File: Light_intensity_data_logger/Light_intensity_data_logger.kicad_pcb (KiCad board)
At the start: 2 copper layers, 23 parts, among them J1 Wire_to_Vbat, Q1 NTJD4001NT1G, Q2 NTJD4001NT1G, U1 BME280, U2 TSL25911FN, U3 TCS34725FN, U4 Teensy3.6

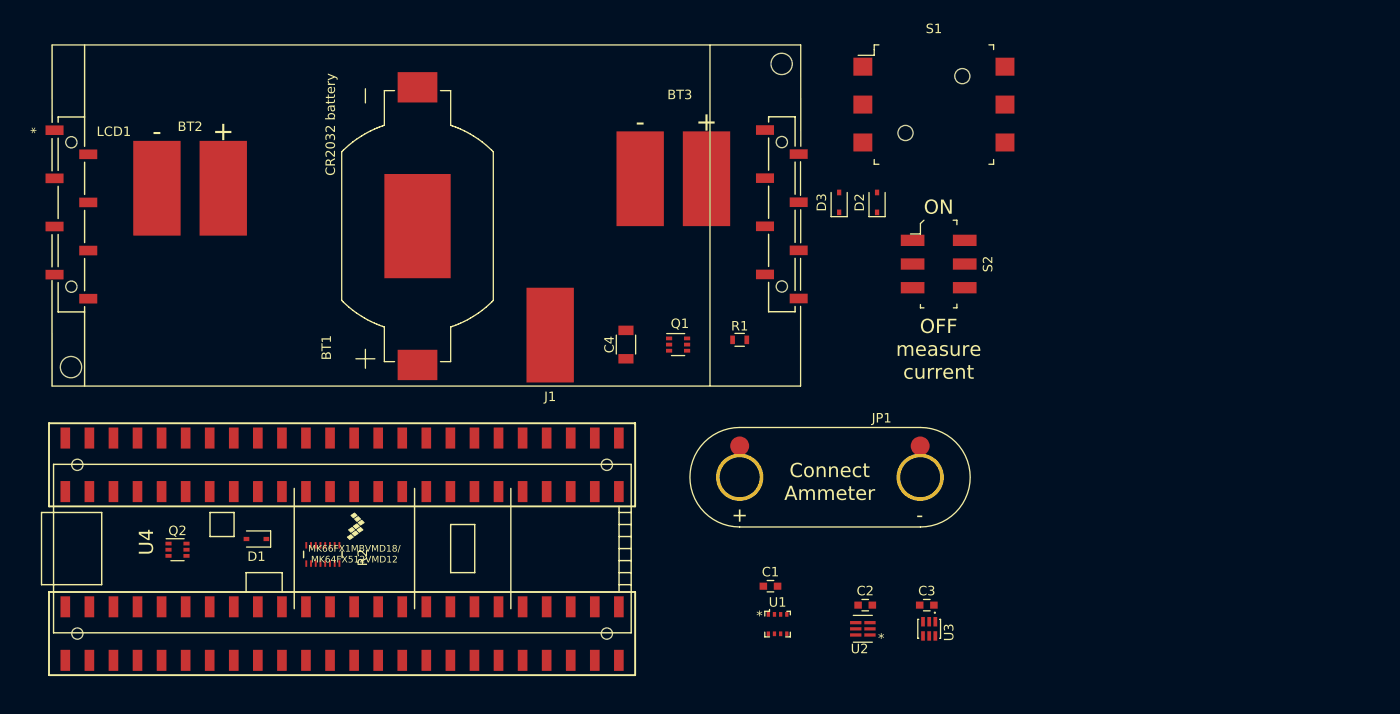
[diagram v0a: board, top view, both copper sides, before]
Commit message: Sensors connected in PCB layout
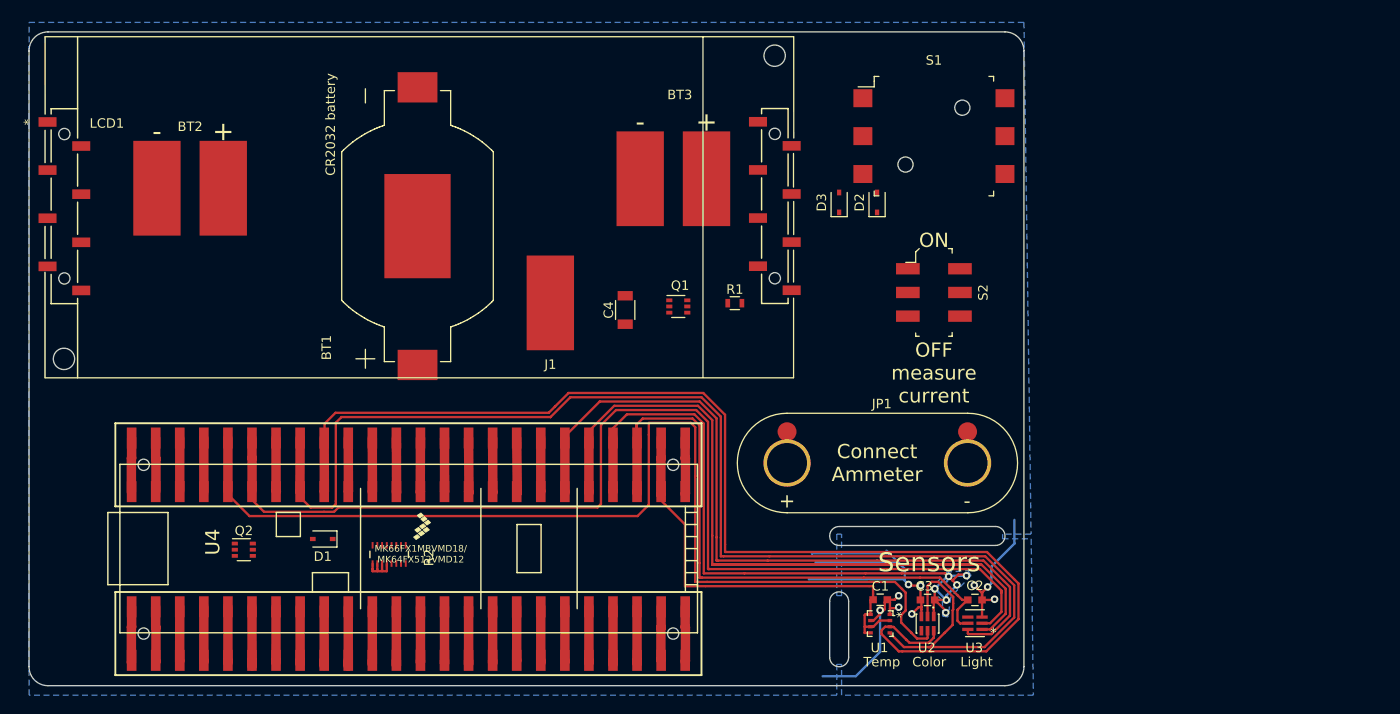
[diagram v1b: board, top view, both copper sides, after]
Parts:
- R2: value EXB-2HV103JV_-_8x10k_resistor_array -> EXB-2HV472JV_-_8x4.7k_resistor_array
- moved U3 11.8 mm to (172.8, 94.4)
- moved C1 11.7 mm to (162.8, 91.9), turned to 180 degrees
- moved C2 11.6 mm to (172.8, 92.0)
- moved U1 10.8 mm to (162.8, 94.5), turned to 270 degrees
- moved D1 7.00 mm to (104.0, 85.5)
- moved Q2 7.00 mm to (95.7, 86.7)
- moved R2 7.00 mm to (111.0, 87.2)
- moved U4 7.00 mm to (82.0, 100.0)
- moved JP1 5.22 mm to (153.0, 77.5)
- moved Q1 4.02 mm to (141.5, 61.0)
- moved R1 3.90 mm to (147.5, 60.6)
- moved C4 3.65 mm to (135.9, 61.4)
- moved J1 3.40 mm to (128.0, 60.6)
- moved S1 3.33 mm to (168.5, 43.0)
- moved S2 3.04 mm to (168.5, 59.5)
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- renumbered U3 to U2, U2 to U3
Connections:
- R2 pad 5: /SDA2 -> /SDA0
- R2 pad 6: /SCL2 -> /SCL0
- U2 pad 2: /SCL2 -> /SCL0
- U2 pad 6: /SDA2 -> /SDA0
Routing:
- net /SCL0: track 0.00 -> 140.5 mm
- net /SCL1: track 0.00 -> 130.9 mm
- net /SDA0: track 0.00 -> 127.1 mm
- net /21*: track 0.00 -> 117.3 mm
- net /22*: track 0.00 -> 112.0 mm
- net GND: track 0.00 -> 89.3 mm, vias 0 -> 9
- net /SDA1: track 0.00 -> 80.0 mm
- net /36: track 0.00 -> 76.5 mm, vias 0 -> 6
- net /35: track 0.00 -> 65.4 mm
- net /34: track 0.00 -> 45.0 mm
- net /3v3: track 0.00 -> 12.1 mm
- net /I2C_Pullup: track 0.00 -> 11.1 mm
- net Net-(U4-Pad10): track 0.00 -> 6.88 mm
- net /SDA2: track 0.00 -> 6.82 mm
- net /7*: track 0.00 -> 6.76 mm
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- added copper zone on B.Cu, net /36
- added copper zone on B.Cu, net GND
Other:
- board outline added: 105 x 69 mm
- board text added: "CUTOUT"
- board text added: "Color"
- board text added: "Light"
- board text added: "Sensors"
- board text added: "Temp"

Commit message: Teensy flipped sensors rewired
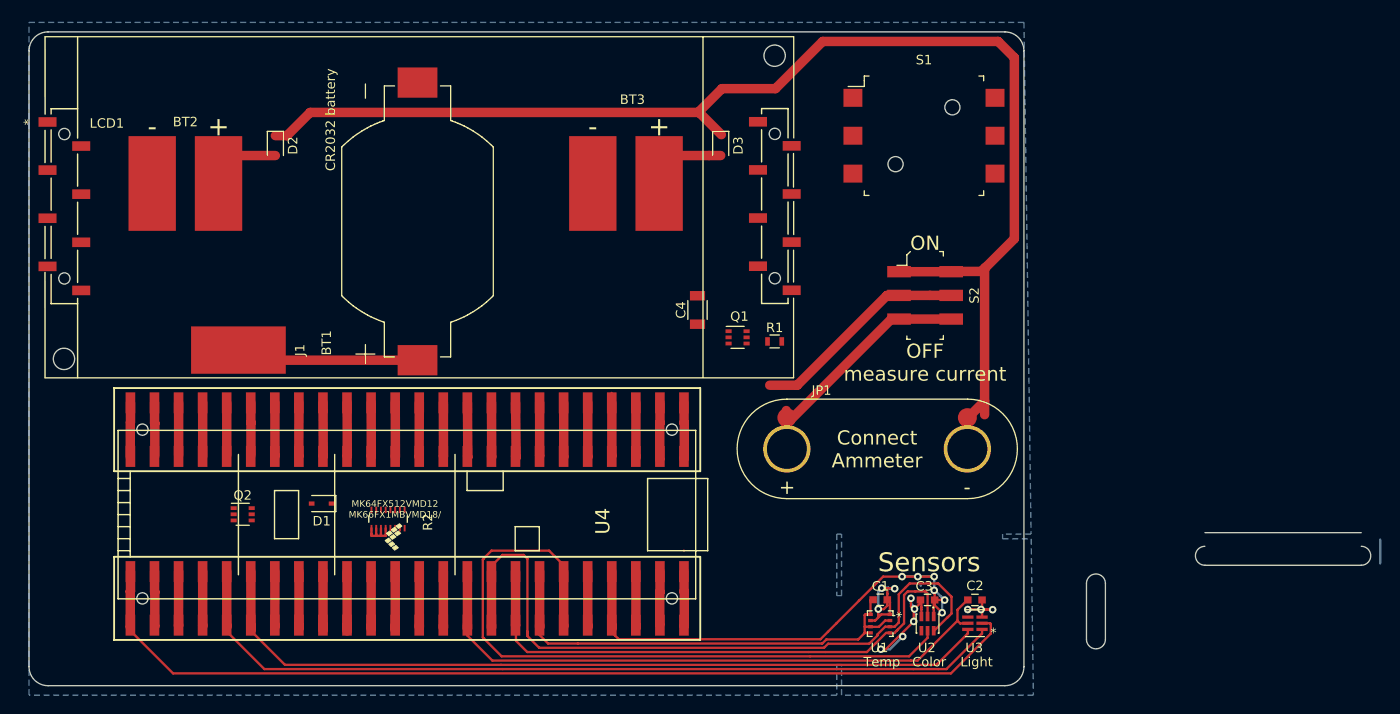
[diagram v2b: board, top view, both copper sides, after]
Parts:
- moved U4 69.0 mm to (143.9, 69.5), turned to 270 degrees
- moved D2 63.8 mm to (99.0, 44.0), turned to 270 degrees
- moved J1 33.3 mm to (95.1, 65.6), turned to 270 degrees
- moved D3 13.9 mm to (146.0, 44.0), turned to 270 degrees
- moved C4 7.63 mm to (143.6, 61.4)
- moved Q1 7.06 mm to (147.8, 64.2)
- moved R1 5.83 mm to (151.7, 64.7)
- moved BT3 5.02 mm to (136.0, 48.0)
- moved Q2 3.74 mm to (95.5, 82.9)
- moved R2 3.74 mm to (110.9, 83.4)
- moved D1 3.74 mm to (103.9, 81.8)
- moved JP1 1.49 mm to (153.0, 76.0)
- moved S1 1.05 mm to (167.4, 43.0)
- moved S2 0.98 mm to (167.6, 59.8)
- moved BT2 0.71 mm to (89.5, 48.0)
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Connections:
- C1 pad 2: /34 -> /20
- C2 pad 1: /35 -> /17
- C3 pad 2: /36 -> /23
- Q2 pad 5: /17 -> /36
- U1 pad 2: /34 -> /20
- U1 pad 5: /34 -> /20
- U1 pad 6: /34 -> /20
- U1 pad 8: /34 -> /20
- U2 pad 1: /36 -> /23
- U2 pad 5: /22* -> /21*
- U3 pad 2: /21* -> /33*
- U3 pad 5: /35 -> /17
- U4 pad 30: Net-(U4-Pad30) -> /33*
- U4 pad 47: Net-(U4-Pad47) -> /20
- U4 pad 50: Net-(U4-Pad50) -> /23
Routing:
- net Net-(D2-Pad1): track 0.00 -> 140.5 mm
- net /22*: track 112.0 -> 6.20 mm
- net /33*: track 0.00 -> 103.0 mm
- net /SCL0: track 140.5 -> 57.7 mm
- net /36: track 76.5 -> 5.98 mm, vias 6 -> 0
- net /17: track 5.66 -> 66.1 mm
- net /35: track 65.4 -> 5.90 mm
- net /23: track 0.00 -> 58.4 mm, vias 0 -> 6
- net /SDA0: track 127.1 -> 74.1 mm
- net /20: track 0.00 -> 49.9 mm
- net /21*: track 117.3 -> 73.9 mm
- net /SCL1: track 130.9 -> 90.2 mm
- net /34: track 45.0 -> 5.80 mm
- net Net-(JP1-Pad1): track 0.00 -> 28.7 mm
- net GND: track 89.3 -> 65.5 mm, vias 9 -> 11
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- removed copper zone on B.Cu, net /36
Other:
- board size 105 x 69 mm -> 141.6 x 69 mm

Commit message: All but left monitor wired
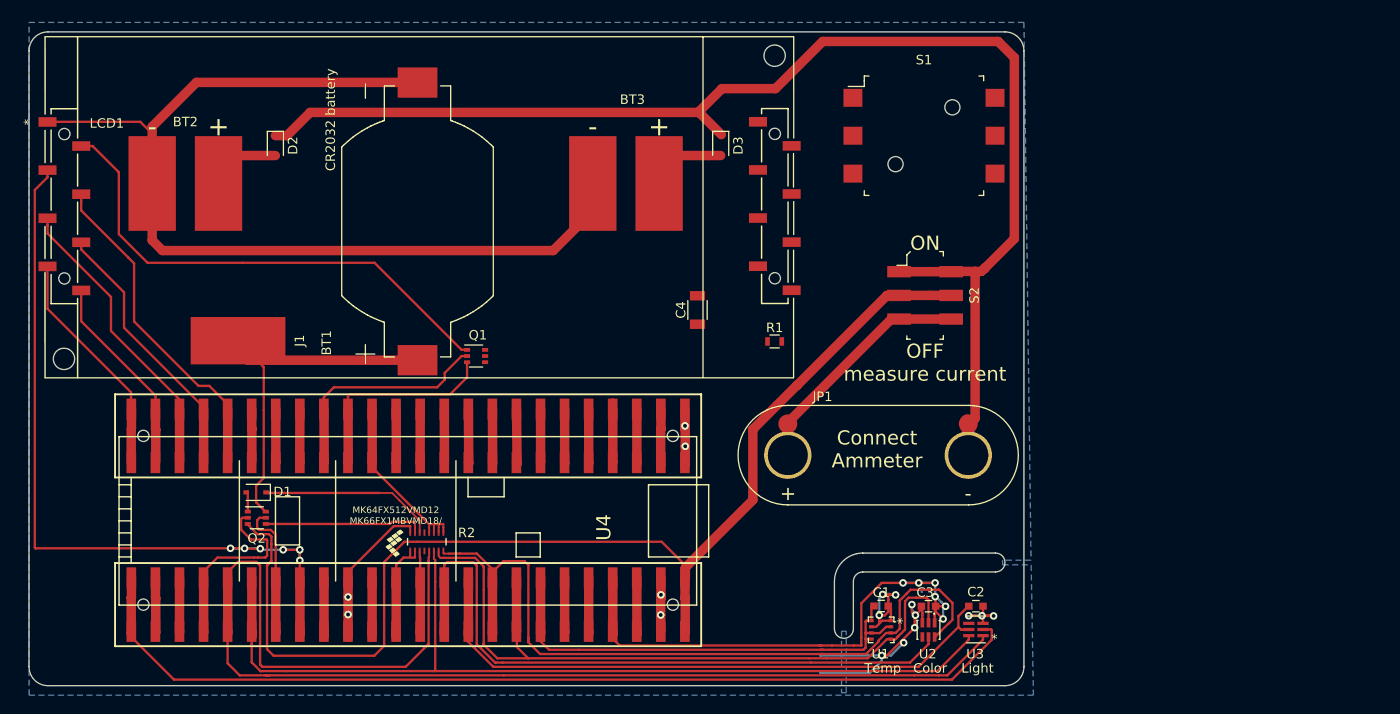
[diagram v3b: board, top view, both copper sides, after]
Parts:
- moved Q1 27.7 mm to (120.2, 66.2)
- moved D1 7.01 mm to (97.0, 80.6)
- moved R2 4.74 mm to (115.0, 85.8), turned to 90 degrees
- moved Q2 1.54 mm to (97.0, 83.3)
- moved J1 0.99 mm to (95.1, 64.6)
- moved JP1 0.67 mm to (153.1, 76.7)
- moved C1 0.67 mm to (162.9, 92.6)
- moved C2 0.67 mm to (172.9, 92.6)
- moved C3 0.67 mm to (167.9, 92.6)
- moved U1 0.67 mm to (162.9, 95.1)
- moved U2 0.67 mm to (167.9, 95.1)
- moved U3 0.67 mm to (172.9, 95.1)
- moved U4 0.67 mm to (144.0, 70.1)
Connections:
- net Net-(U4-Pad10) renamed /8
- Q1 pad 2: /5 -> /24
- Q2 pad 1: Net-(BT1-Pad+) -> Net-(D1-Pad2)
- Q2 pad 2: /16* -> /36
- Q2 pad 5: /36 -> /39
- Q2 pad 6: Net-(D1-Pad2) -> Net-(BT1-Pad+)
- R2 pad 1: /A1 -> /A0
- R2 pad 2: /A1 -> /A0
- R2 pad 3: /A0 -> /A1
- R2 pad 5: /SDA0 -> /SCL1
- R2 pad 6: /SCL0 -> /SDA1
- R2 pad 7: /SCL1 -> /SCL0
- R2 pad 8: /SDA1 -> /SDA0
- U2 pad 5: /21* -> /16*
- U4 pad 16: /DB0 -> /24
- U4 pad 17: /DB1 -> Net-(U4-Pad17)
- U4 pad 18: /DB2 -> Net-(U4-Pad18)
- U4 pad 19: /DB3 -> Net-(U4-Pad19)
- U4 pad 2: /RS -> Net-(U4-Pad2)
- U4 pad 20: /DB4 -> /RS
- U4 pad 21: /DB5 -> /E
- U4 pad 22: /DB6 -> /RW
- U4 pad 23: /DB7 -> /DB1
- U4 pad 24: /E -> /DB0
- U4 pad 3: /RW -> Net-(U4-Pad3)
- U4 pad 36: Net-(U4-Pad36) -> /39
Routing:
- net GND: track 65.5 -> 195.5 mm, vias 11 -> 17
- net /Vin: track 28.9 -> 123.3 mm
- net /DAC0: track 6.38 -> 84.1 mm, vias 0 -> 6
- net /21*: track 73.9 -> 7.07 mm
- net /16*: track 6.34 -> 71.0 mm
- net Net-(LCD1-Pad2): track 0.00 -> 53.5 mm
- net /SCL1: track 90.2 -> 136.6 mm
- net /RS: track 6.00 -> 35.4 mm
- net /RW: track 5.92 -> 31.7 mm
- net /24: track 0.00 -> 24.3 mm
- net /E: track 5.71 -> 28.5 mm
- net Net-(BT1-Pad+): track 18.9 -> 41.5 mm
- net /SCL0: track 57.7 -> 77.0 mm
- net Net-(D1-Pad1): track 0.00 -> 18.9 mm
- net /DB0: track 5.67 -> 24.5 mm
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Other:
- board size 141.6 x 69 mm -> 105 x 69 mm
- board text removed: "Sensors"

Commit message: Complete routed draft - pass DRC other than courtyard
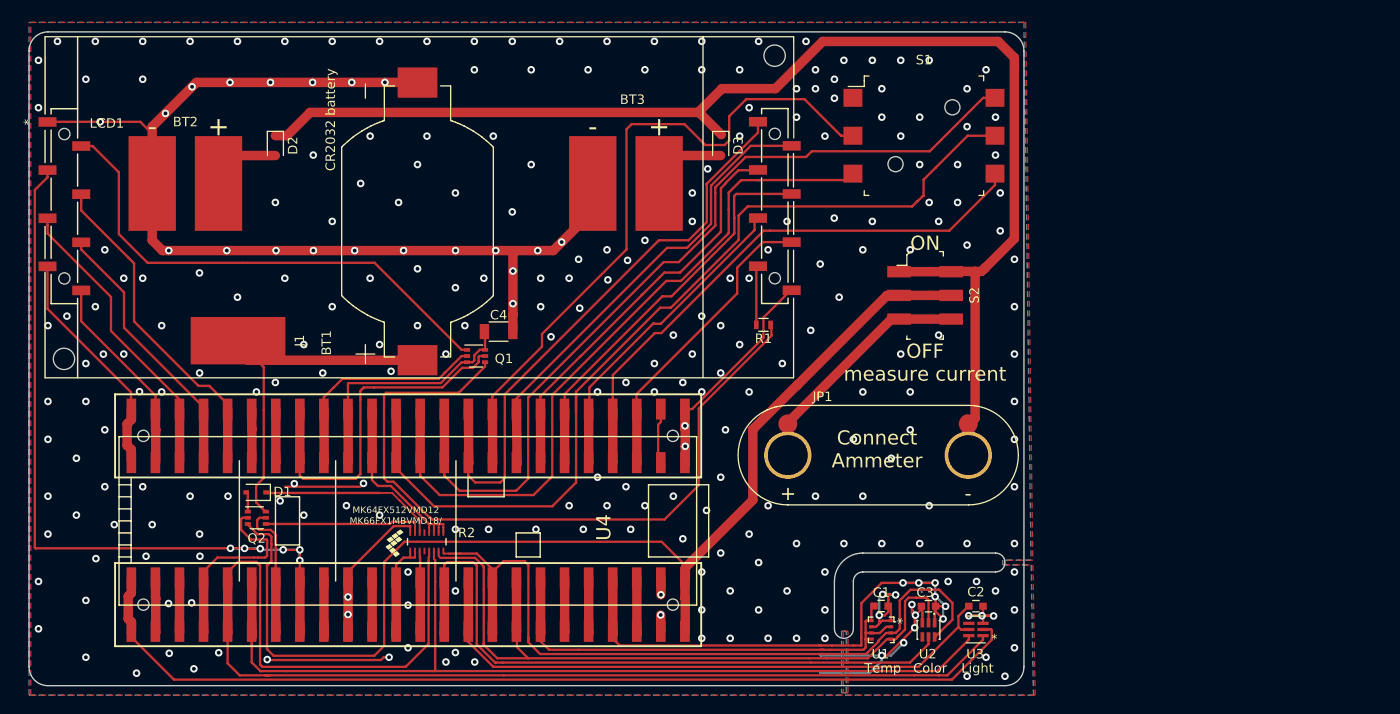
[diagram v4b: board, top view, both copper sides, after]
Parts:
- moved C4 21.1 mm to (122.6, 63.6), turned to 0 degrees
- moved R1 2.11 mm to (150.5, 62.9), turned to 180 degrees
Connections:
- Q1 pad 5: /2* -> /25
- S1 pad 2: /6* -> /7*
- S1 pad 3: /7* -> /10*
- S1 pad 5: /10* -> /11*
- S1 pad 6: /11* -> /2*
- U4 pad 10: /8 -> /DB2
- U4 pad 17: Net-(U4-Pad17) -> /25
- U4 pad 3: Net-(U4-Pad3) -> /DB7
- U4 pad 5: /SCL2 -> /DB6
- U4 pad 51: /3v3 -> Net-(U4-Pad51)
- U4 pad 6: /SDA2 -> /DB5
- U4 pad 7: /5 -> /DB4
- U4 pad 8: /6* -> /DB3
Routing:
- net /11*: track 5.80 -> 97.4 mm
- net /9*: track 5.67 -> 90.4 mm
- net Net-(Q1-Pad4): track 0.00 -> 77.8 mm
- net /10*: track 5.76 -> 75.6 mm
- net /7*: track 5.84 -> 71.4 mm
- net /DB2: track 0.00 -> 62.2 mm
- net /2*: track 6.75 -> 61.4 mm
- net /DB3: track 0.00 -> 49.7 mm
- net GND: track 195.5 -> 240.4 mm, vias 17 -> 279
- net /DB5: track 0.00 -> 43.7 mm
- net /DB4: track 0.00 -> 42.8 mm
- net /25: track 0.00 -> 37.6 mm
- net /DB6: track 0.00 -> 34.9 mm
- net /DB7: track 0.00 -> 32.0 mm
- net Net-(U4-Pad51): track 0.00 -> 6.30 mm
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- added copper zone on F.Cu, net GND

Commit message: First draft complete
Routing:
- net Net-(U4-Pad2): track 5.99 -> 17.2 mm
- net GND: track 240.4 -> 246.1 mm, vias 279 -> 298
- added copper zone on B.Cu, net /23
- added copper zone on F.Cu, net /23
- added copper zone on B.Cu, net /DAC0
- added copper zone on F.Cu, net /DAC0
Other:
- board text added: "*"
- board text added: "G 0 1 2 3 4 5 6 7 8 9 10 11 12 3v3 24 25 26 27 28 29 30 31 32"
- board text added: "Vin AG 3v3 23 22 21 20 19 18 17 16 15 14 13 G D1 D0 39 38 37 36 35 34 33"

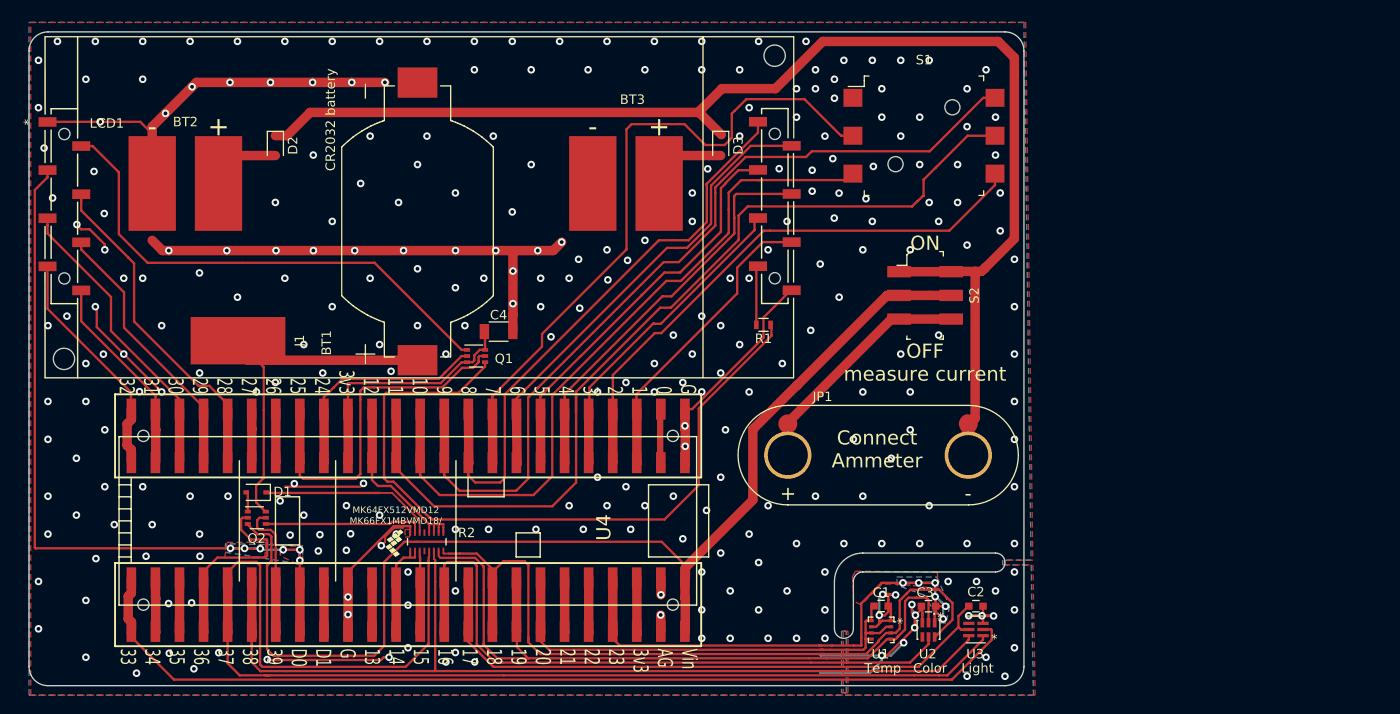
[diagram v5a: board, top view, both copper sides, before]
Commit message: Vias optimized
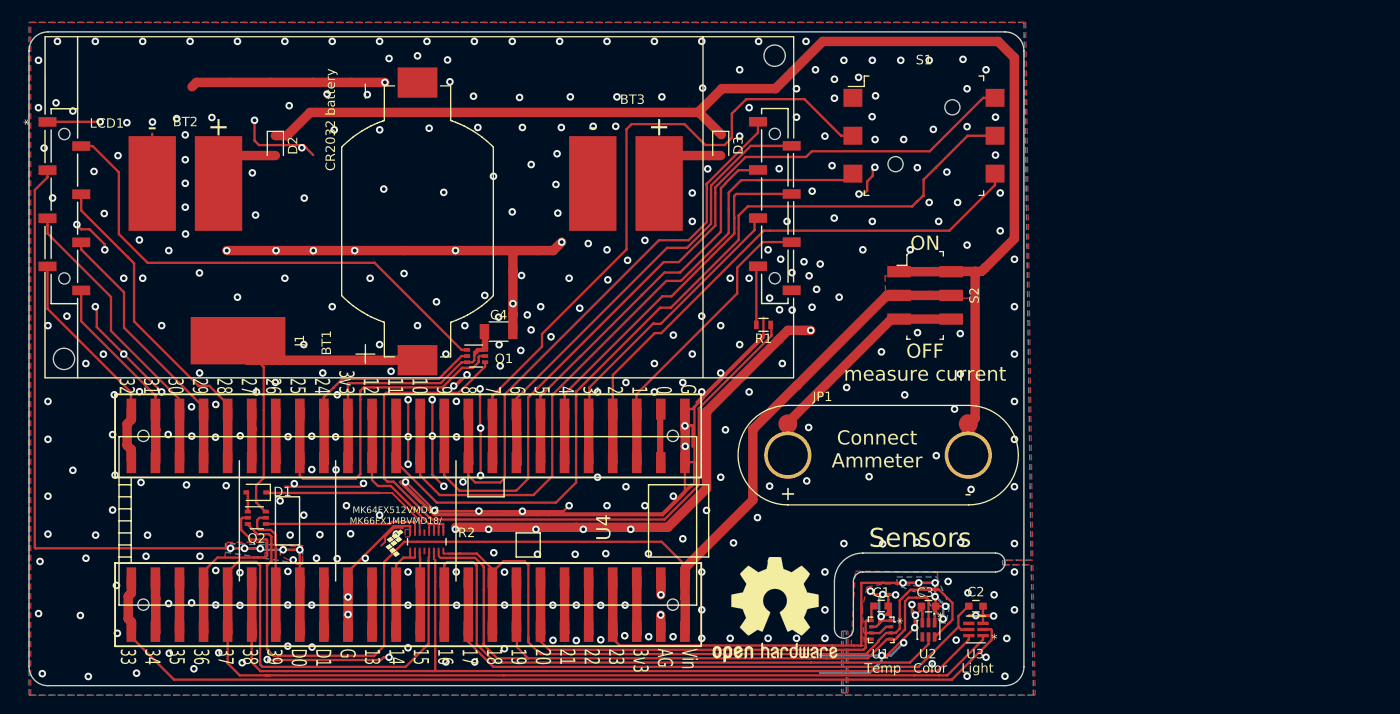
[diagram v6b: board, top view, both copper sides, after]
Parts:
- added REF***: OSHW-Logo2_14.6x12mm_SilkScreen, Symbols:OSHW-Logo2_14.6x12mm_SilkScreen, F.Cu at (151.7, 93.0)
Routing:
- net GND: track 246.1 -> 429.6 mm, vias 298 -> 392
- net /3v3: track 26.4 -> 31.8 mm
- net /23: track 61.2 -> 62.7 mm
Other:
- board text added: "Sensors"
